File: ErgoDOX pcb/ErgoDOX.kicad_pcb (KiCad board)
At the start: 2 copper layers, 182.8 x 142.1 mm, 47 parts, among them SW0:10 SW0:3, SW0:11 SW0:2, SW0:12 SW0:1, SW0:7 SW0:6, SW0:8 SW0:5, SW0:9 SW0:4, SW1:10 SW1:3, SW1:11 SW1:2, SW1:12 SW1:1, SW1:13 SW1:0, SW1:9 SW1:4, SW2:10 SW2:3, SW2:11 SW2:2, SW2:12 SW2:1, SW2:13 SW2:0, SW2:7 SW2:6, SW2:8 SW2:5, SW2:9 SW2:4, SW3:10 SW3:3, SW3:11 SW3:2, SW3:12 SW3:1, SW3:13 SW3:0, SW3:8 SW3:5, SW3:9 SW3:4, SW4:10 SW4:3, SW4:11 SW4:2, SW4:12 SW4:1, SW4:13 SW4:0, SW4:7 SW4:6, SW4:8 SW4:5, SW4:9 SW4:4, SW5:10 SW5:3, SW5:11 SW5:2, SW5:12 SW5:1, SW5:13 SW5:0, SW5:7 SW5:6, SW5:8 SW5:5, SW5:9 SW5:4, U1 nice!nano

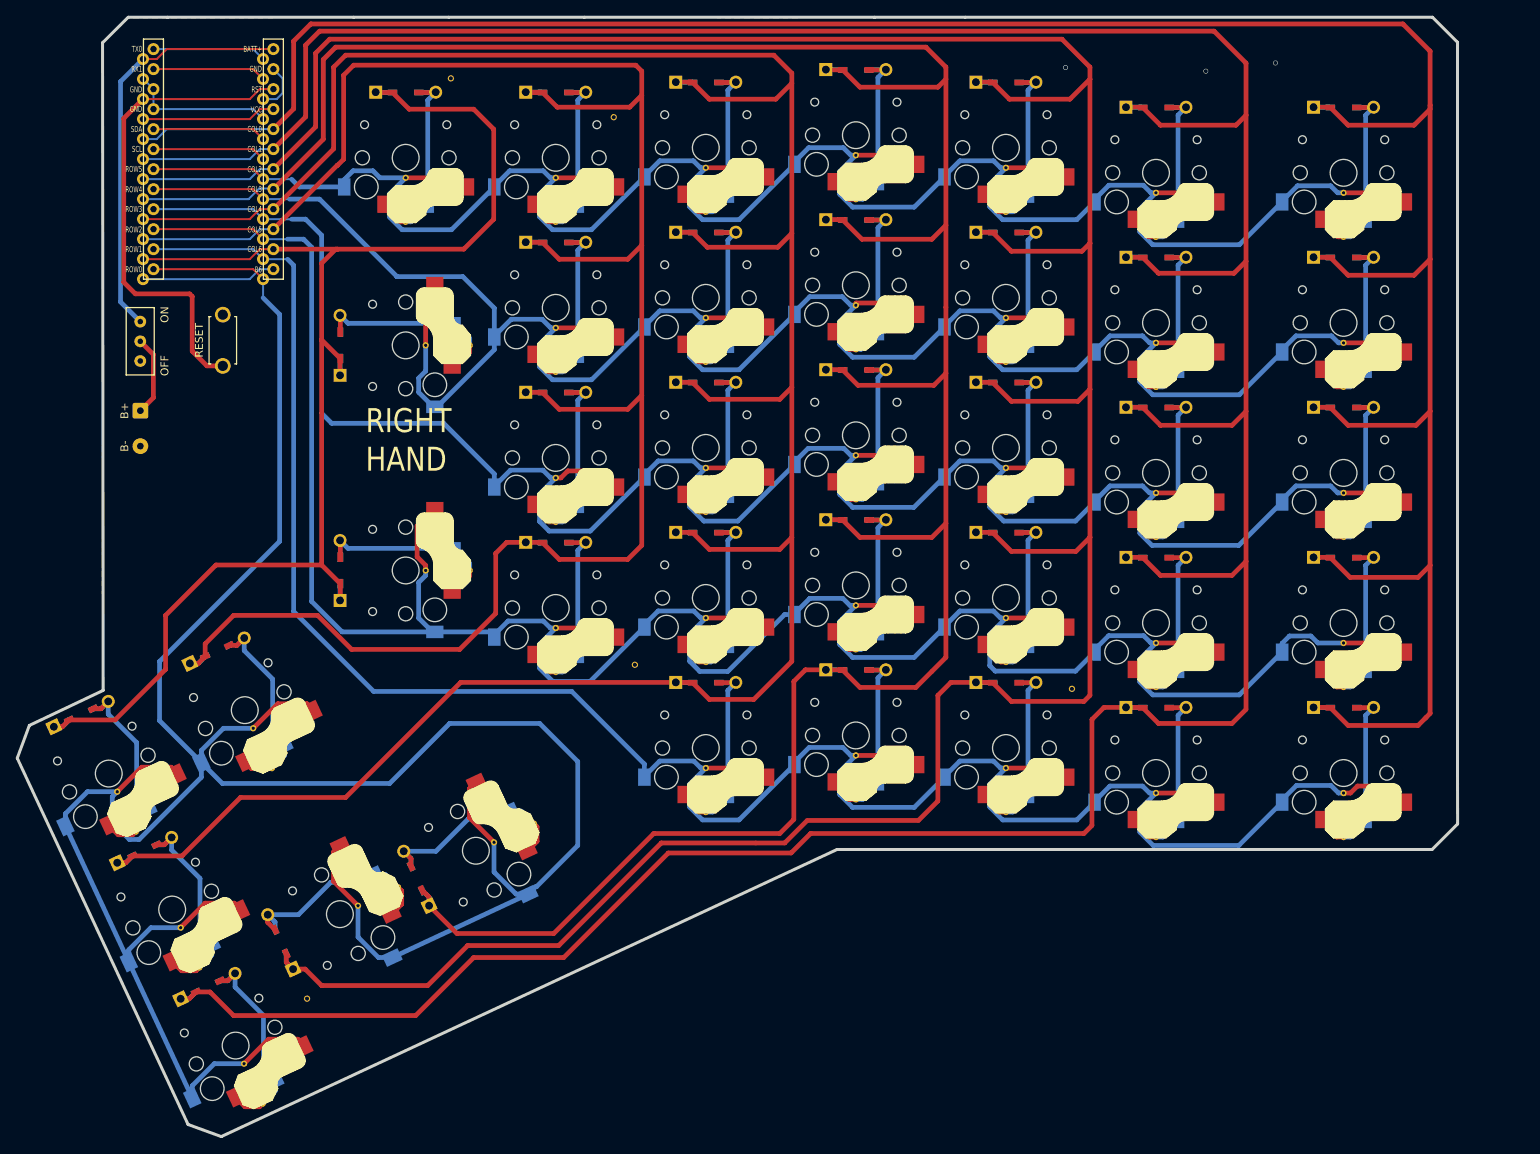
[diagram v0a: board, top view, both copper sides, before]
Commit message: update holes
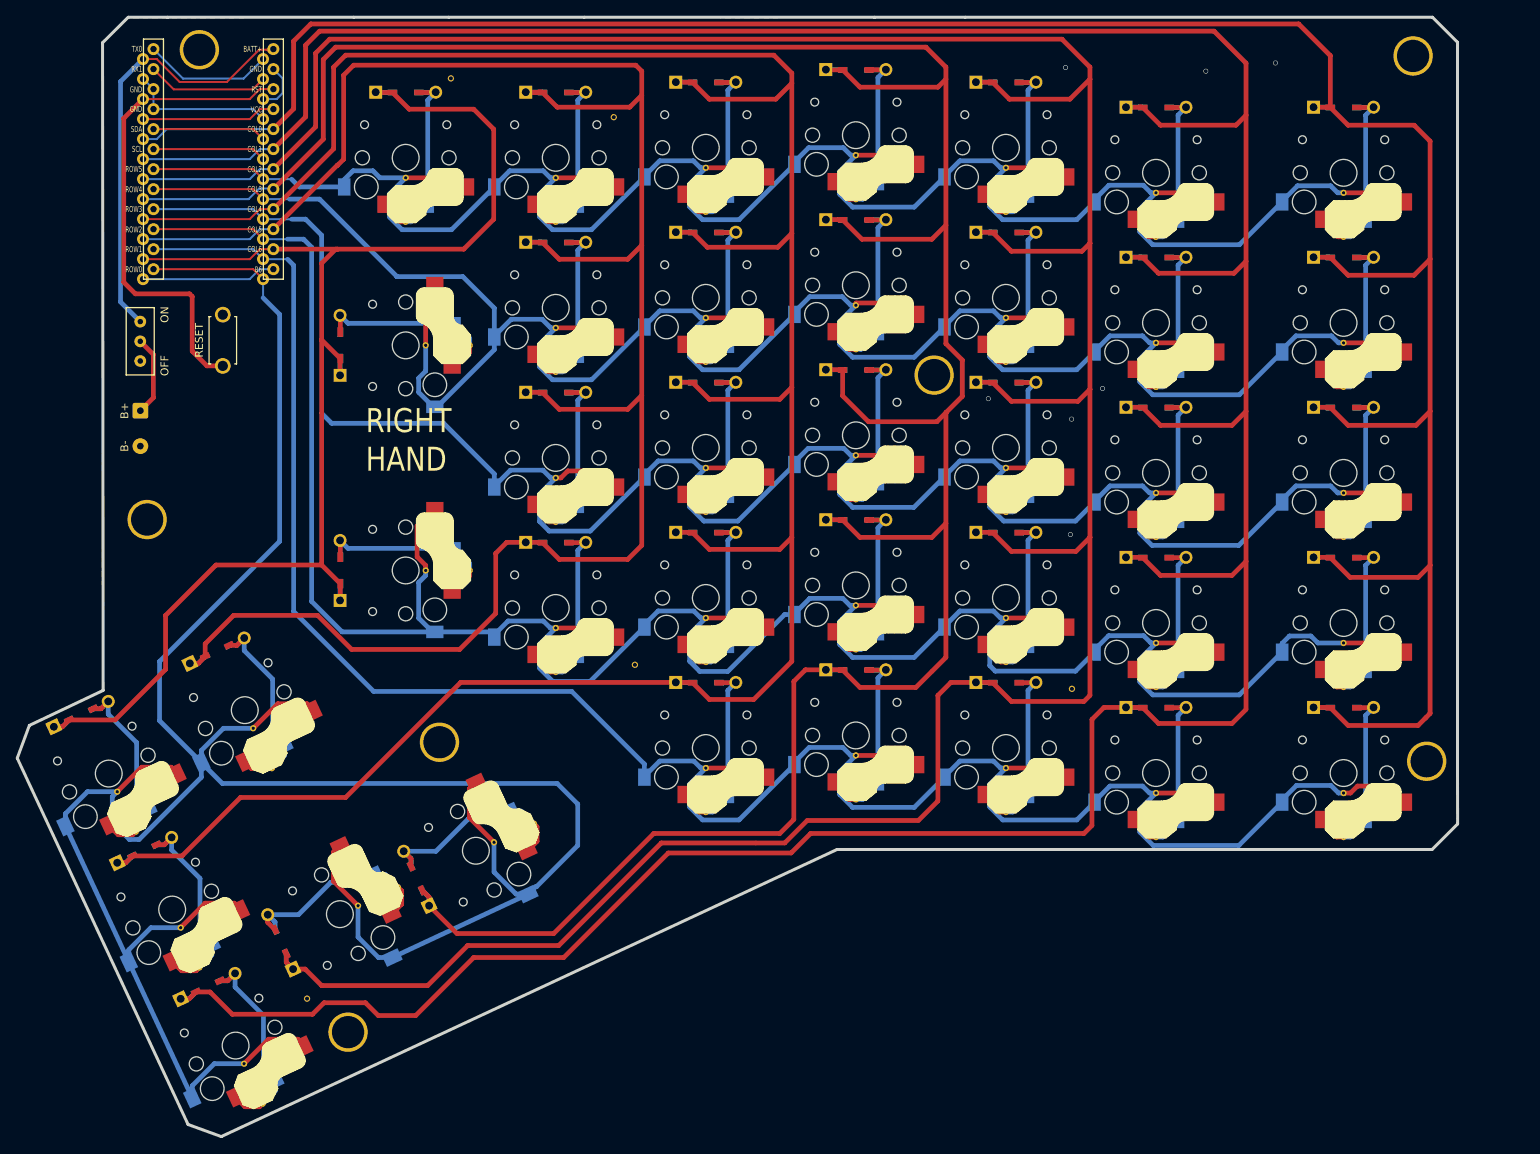
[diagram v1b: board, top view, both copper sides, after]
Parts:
- added ?: , , F.Cu at (139.5, 92.7)
- added ?: , , F.Cu at (65.1, 176.1)
- added ?: , , F.Cu at (46.2, 51.4)
- added ?: , , F.Cu at (39.6, 111.0)
- added ?: , , F.Cu at (202.0, 141.7)
- added ?: , , F.Cu at (200.3, 52.2)
- added ?: , , F.Cu at (76.7, 139.3)
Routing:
- net /COL0: track 353.2 -> 335.4 mm
- net /ROW0: track 348.9 -> 339.4 mm
- net /COL10: track 367.5 -> 373.0 mm
- net +BATT: track 52.6 -> 54.7 mm
- net NET-(U3-PAD1): track 14.4 -> 16.5 mm
- net /COL1: track 478.1 -> 479.3 mm
- net NET-(U3-PAD2): track 14.4 -> 15.5 mm
- net GND: vias 3 -> 7

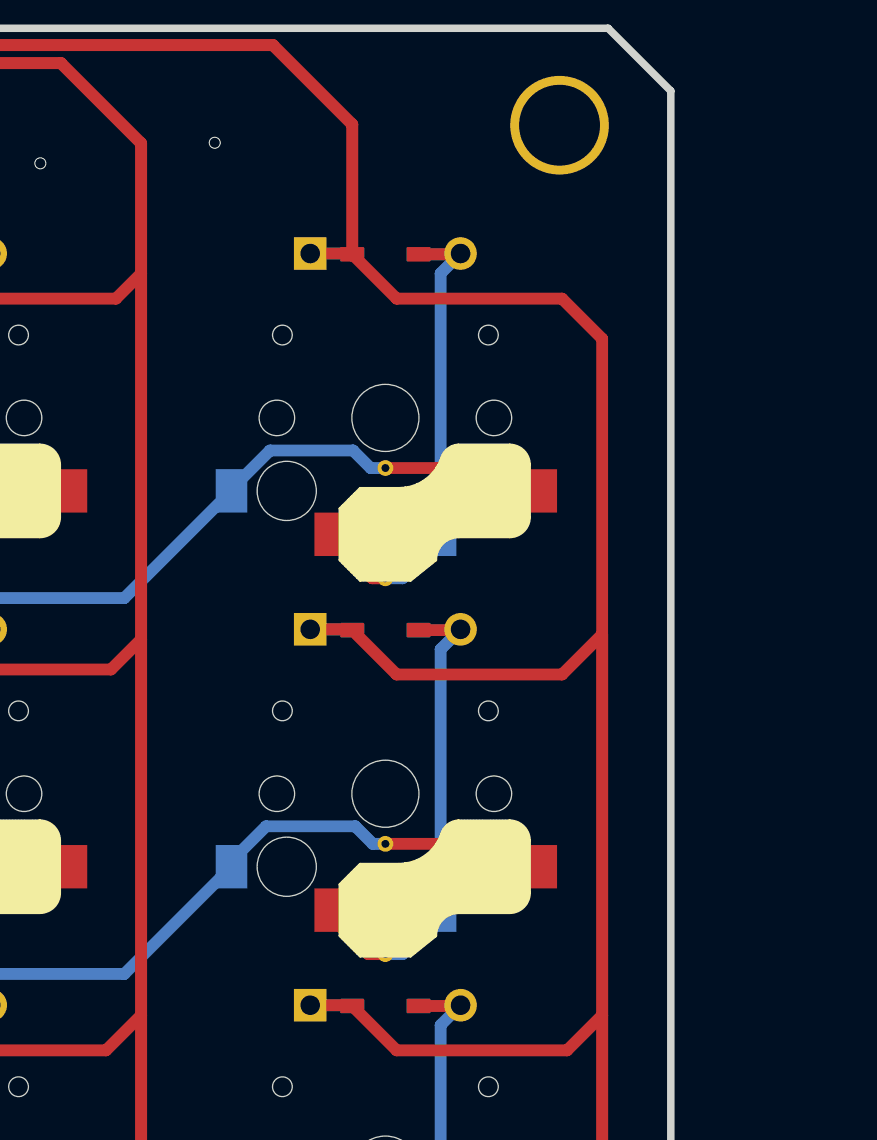
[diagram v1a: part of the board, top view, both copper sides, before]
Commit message: create 1u1.5u footprint
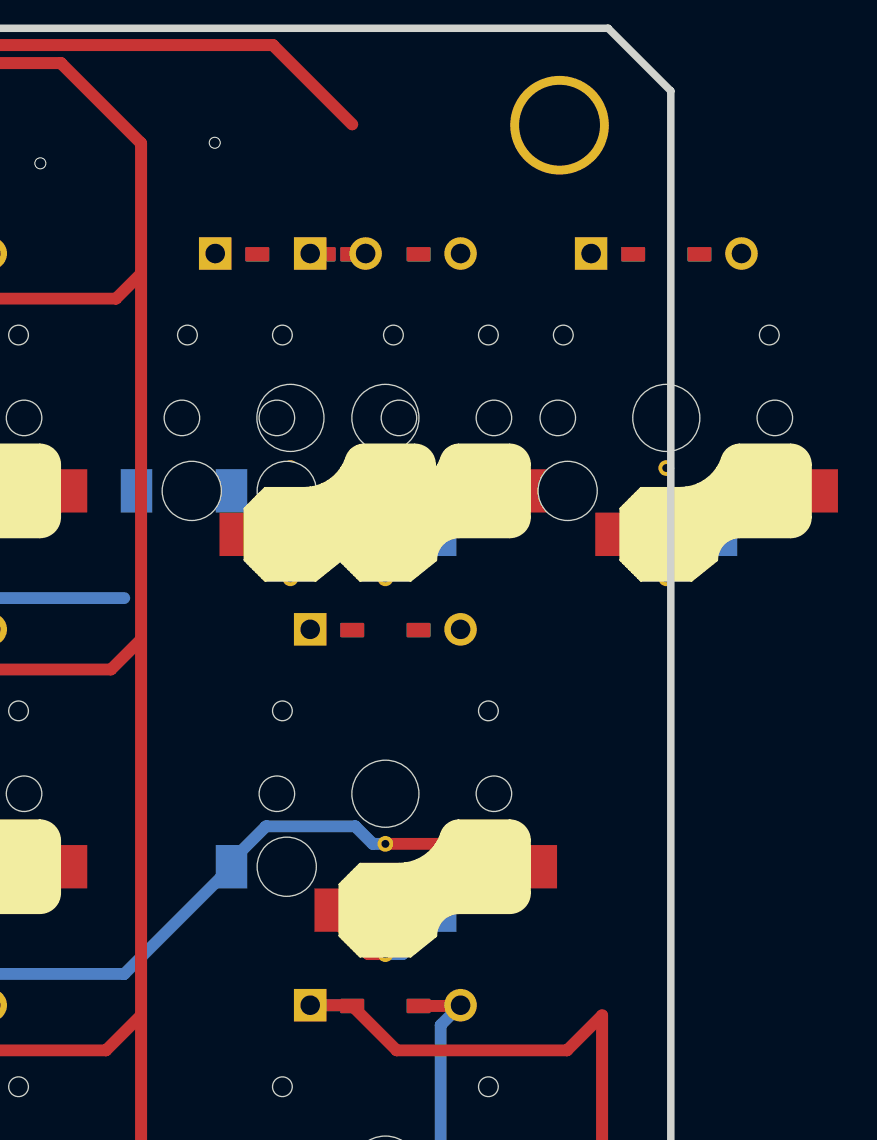
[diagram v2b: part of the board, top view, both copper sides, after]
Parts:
- SW5:13: footprint ErgoDOX pcb:Choc_Hotswap -> ErgoDOX pcb:Choc_Hotswap_1u1.5u
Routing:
- net /COL0: track 335.4 -> 257.3 mm
- net Net-(SW5:13-Pad2): track 26.1 -> 0.00 mm
- net /ROW5: track 288.5 -> 262.8 mm
- net Net-(SW4:13-Pad2): track 26.0 -> 7.20 mm

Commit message: Revert "create 1u1.5u footprint"
This reverts commit 3dfe5ebad1ff0df9ab9336540538172015dde196.
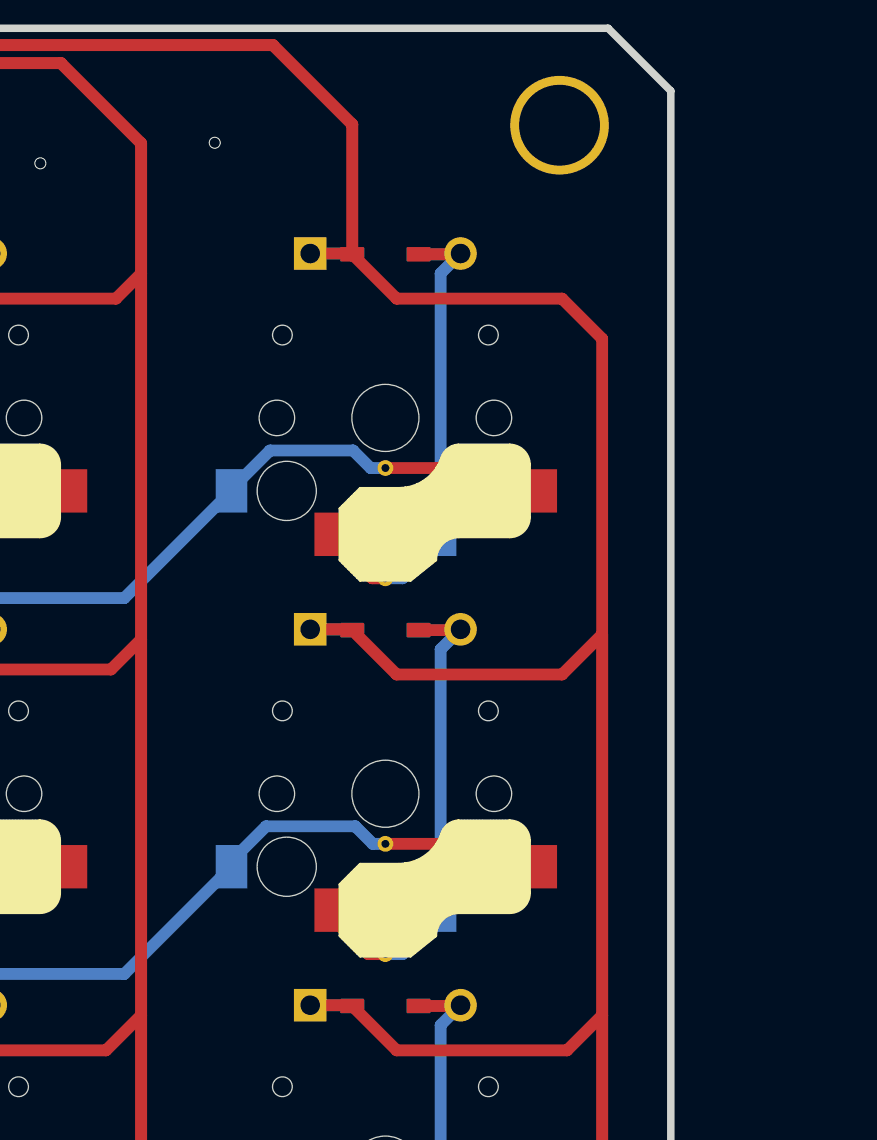
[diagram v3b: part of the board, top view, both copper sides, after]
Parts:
- SW5:13: footprint ErgoDOX pcb:Choc_Hotswap_1u1.5u -> ErgoDOX pcb:Choc_Hotswap
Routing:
- net /COL0: track 257.3 -> 335.4 mm
- net Net-(SW5:13-Pad2): track 0.00 -> 26.1 mm
- net /ROW5: track 262.8 -> 288.5 mm
- net Net-(SW4:13-Pad2): track 7.20 -> 26.0 mm
